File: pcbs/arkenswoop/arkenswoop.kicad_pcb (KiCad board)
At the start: 2 copper layers, 108.1 x 88.5 mm, 68 parts, among them J1 TRRS, SW1 Choc, SW10 Choc, SW11 Choc, SW12 Choc, SW13 Choc, SW14 Choc, SW15 Choc, SW16 Choc, SW17 Choc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

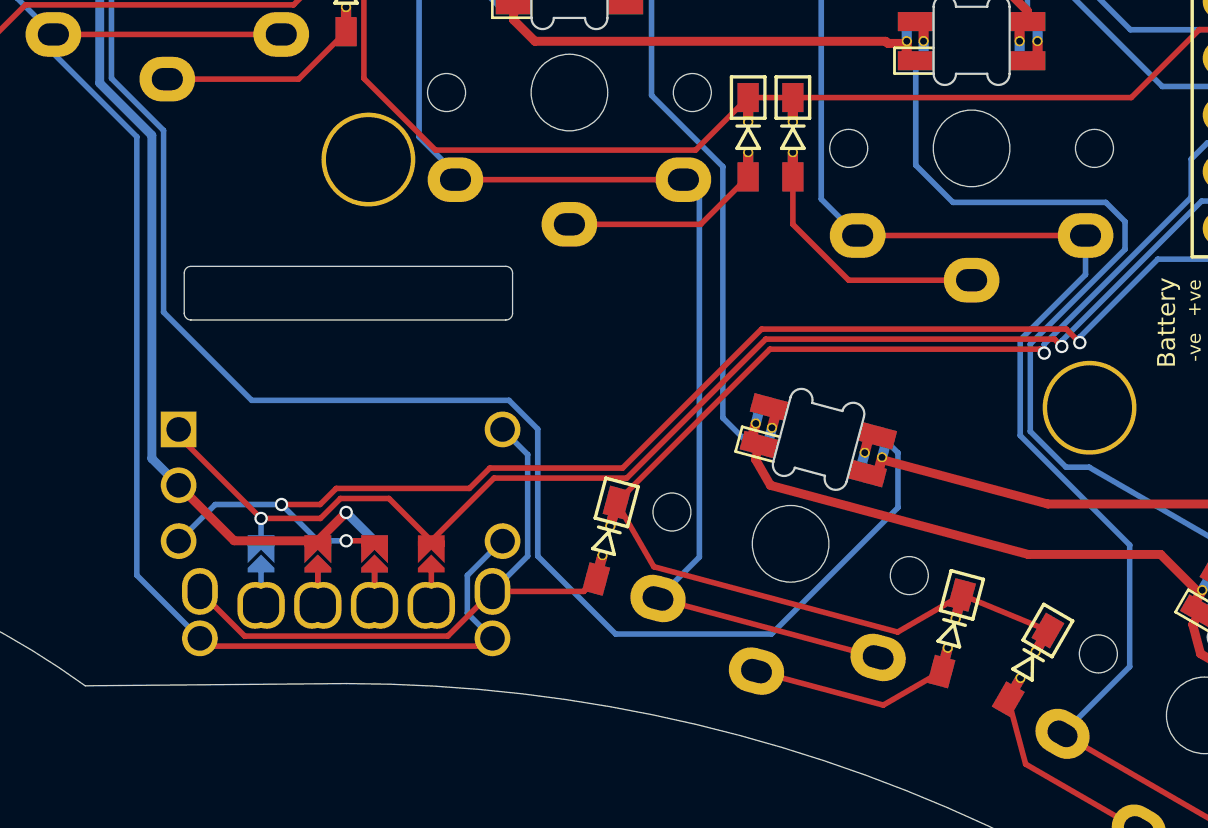
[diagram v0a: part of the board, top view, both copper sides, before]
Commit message: moving the encoder about 0.3mm down ; this should give enough clearance to the nearest key and its keycap
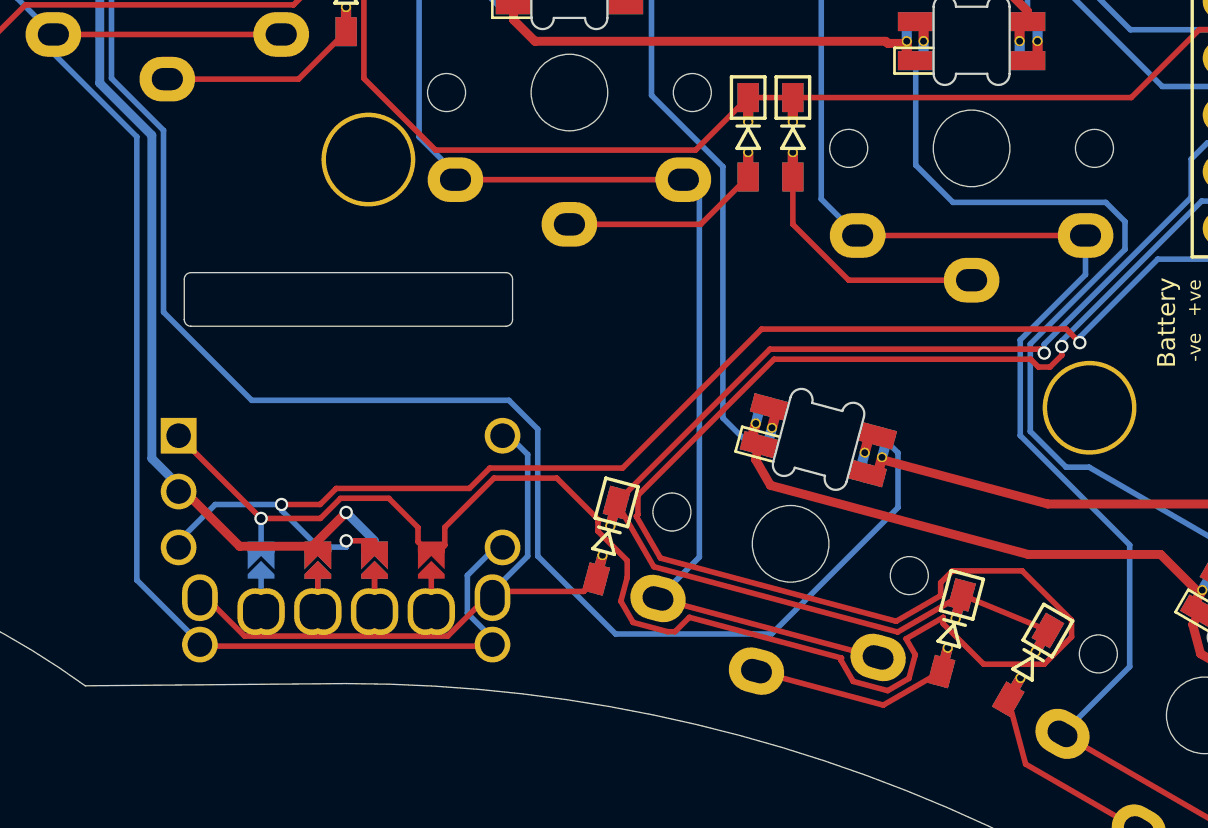
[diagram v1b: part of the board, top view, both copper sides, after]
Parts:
- moved EN1 0.28 mm to (115.2, 127.6)
- moved EN2 0.28 mm to (115.2, 127.6)
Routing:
- net eda: track 73.5 -> 129.1 mm
- net edb: track 74.2 -> 75.1 mm

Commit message: removed leds footprint
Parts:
- removed L1, L10, L11, L12, L13, L14, L15, L16, L17, L2, L3, L4, L5, L6, L7, L8, L9: SK6812Mini-e, swoop:SK6812_Mini_E
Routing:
- net VCC: track 394.7 -> 48.2 mm, vias 6 -> 3
- net GND: track 498.0 -> 160.6 mm, vias 8 -> 7
- net Net-(L13-Pad4): track 69.3 -> 0.00 mm
- net eda: track 129.1 -> 74.7 mm
- net led: track 63.9 -> 12.1 mm
- net Net-(L15-Pad4): track 42.9 -> 0.00 mm
- net Net-(L11-Pad4): track 35.2 -> 0.00 mm
- net Net-(L2-Pad4): track 31.0 -> 0.00 mm
- net Net-(L4-DIN): track 30.0 -> 0.00 mm
- net Net-(L14-Pad2): track 24.4 -> 0.00 mm
- net Net-(L14-Pad4): track 23.4 -> 0.00 mm
- net Net-(L2-Pad2): track 23.4 -> 0.00 mm
- net Net-(L4-Pad2): track 23.4 -> 0.00 mm
- net Net-(L12-Pad4): track 23.4 -> 0.00 mm
- net Net-(L10-Pad2): track 17.4 -> 0.00 mm
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
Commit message: customized pcb to have the jlcpcb order number under the mcu
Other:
- board text added: "Arkenswoop v0.5.0 https://github.com/SuperFola/arkenswoop"
- board text added: "JLCJLCJLCJLC"
- board text removed: "Arkenswoop v0.4.2 https://github.com/SuperFola/arkenswoop"
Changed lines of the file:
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@@
   (paper "A4")
   (title_block
-    (title "Swoop Choc")
-    (date "2023-05-28")
-    (rev "0.4.2")
-    (company "jmnw")
+    (title "Arkenswoop")
+    (date "2023-06-12")
+    (rev "0.5.0")
+    (company "SuperFola")
   )
   (layers
@@
   (gr_arc (start 80.677686 69.000074) (mid 81.223519 67.756064) (end 82.48217 67.244898)
     (stroke (width 0.05) (type solid)) (layer "Edge.Cuts"))
-  (gr_text "Arkenswoop v0.4.2\nhttps://github.com/SuperFola/arkenswoop" (at 163.188328 89.953937 90) (layer "B.SilkS")
+  (gr_text "Arkenswoop v0.5.0\nhttps://github.com/SuperFola/arkenswoop" (at 163.188328 89.953937 90) (layer "B.SilkS")
     (effects (font (size 0.8 0.8) (thickness 0.1)) (justify left mirror))
   )
-  (gr_text "Arkenswoop v0.4.2\nhttps://github.com/SuperFola/arkenswoop" (at 163.188327 114.013939 90) (layer "F.SilkS")
+  (gr_text "JLCJLCJLCJLC" (at 161.22 113.85 90) (layer "F.SilkS")
+    (effects (font (size 0.9 0.9) (thickness 0.1)) (justify left bottom))
+  )
+  (gr_text "Arkenswoop v0.5.0\nhttps://github.com/SuperFola/arkenswoop" (at 163.188327 114.013939 90) (layer "F.SilkS")
     (effects (font (size 0.8 0.8) (thickness 0.1)) (justify left))
   )

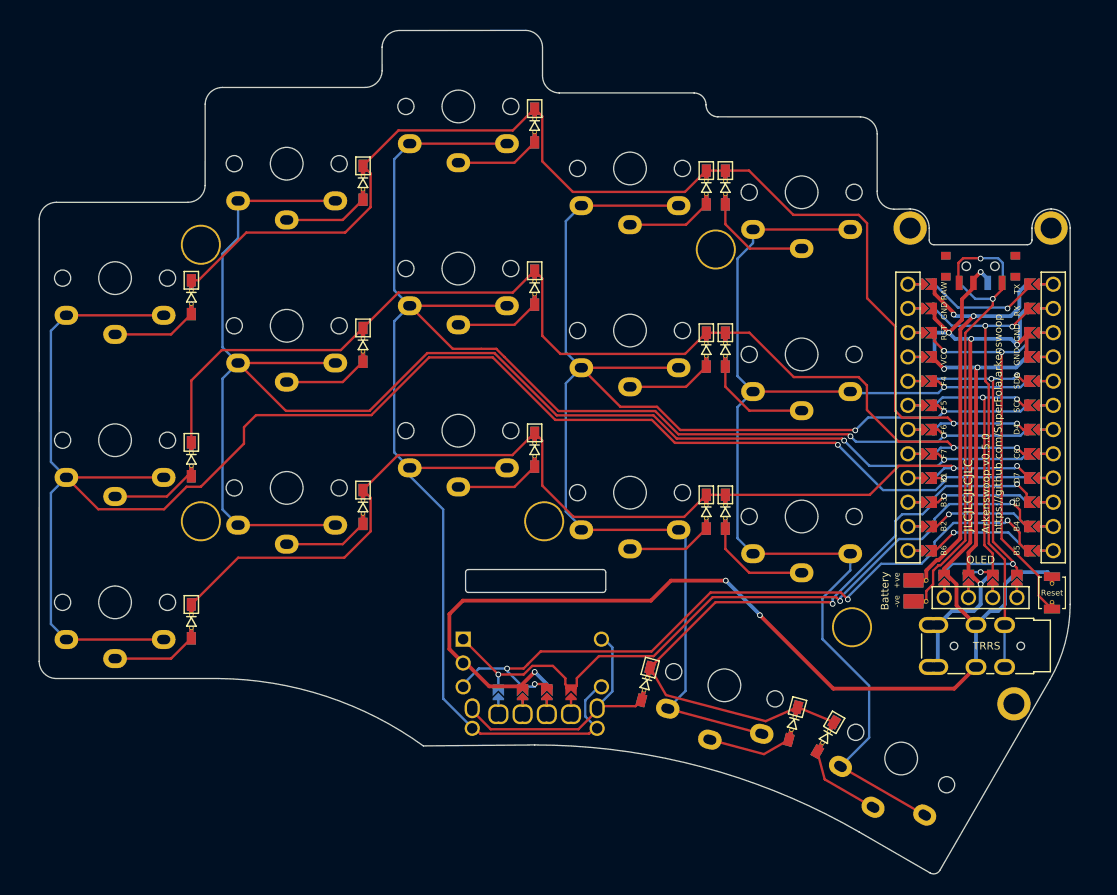
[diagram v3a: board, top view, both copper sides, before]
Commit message: removing old soldered version
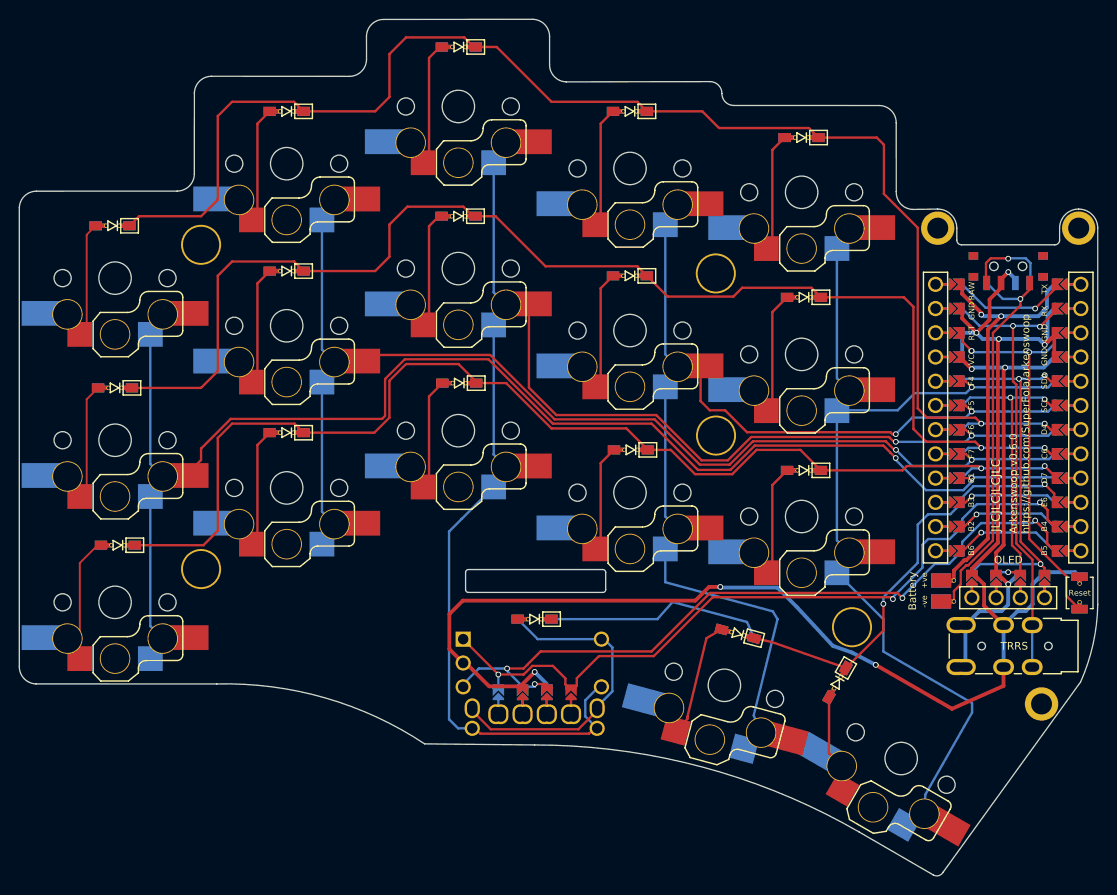
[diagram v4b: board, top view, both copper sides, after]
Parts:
- SW1, SW10, SW11, SW12, SW13, SW14, SW15, SW16, SW17, SW2, SW3, SW4, SW5, SW6, SW7, SW8, SW9: footprint swoop:Choc -> Library:Kailh-pg1350-socket-reversible
- moved H4 20.1 mm to (134.2, 103.8)
- moved ED1 13.5 mm to (115.2, 123.0), turned to 180 degrees
- moved D3 11.5 mm to (107.3, 63.0), turned to 180 degrees
- moved D4 11.3 mm to (125.2, 69.8), turned to 180 degrees
- moved D12 11.2 mm to (89.2, 103.5), turned to 180 degrees
- moved D1 11.1 mm to (71.0, 81.8), turned to 180 degrees
- moved D7 11.1 mm to (89.2, 86.5), turned to 180 degrees
- moved D9 11.1 mm to (125.2, 87.0), turned to 180 degrees
- moved D11 11.1 mm to (71.5, 115.2), turned to 180 degrees
- moved D16 11.0 mm to (136.5, 124.5), turned to 165 degrees
- moved D2 11.0 mm to (89.2, 69.8), turned to 180 degrees
- moved D6 11.0 mm to (71.2, 98.8), turned to 180 degrees
- moved D8 10.9 mm to (107.2, 80.8), turned to 180 degrees
- moved D13 10.6 mm to (107.3, 98.2), turned to 180 degrees
- moved D14 10.2 mm to (125.3, 105.2), turned to 180 degrees
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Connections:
- D1 pad 2: (no net) -> Net-(D1-A)
- D10 pad 2: (no net) -> Net-(D10-A)
- D11 pad 2: (no net) -> Net-(D11-A)
- D12 pad 2: (no net) -> Net-(D12-A)
- D13 pad 2: (no net) -> Net-(D13-A)
- D14 pad 2: (no net) -> Net-(D14-A)
- D15 pad 2: (no net) -> Net-(D15-A)
- D16 pad 2: (no net) -> Net-(D16-A)
- D17 pad 2: (no net) -> Net-(D17-A)
- D2 pad 2: (no net) -> Net-(D2-A)
- D3 pad 2: (no net) -> Net-(D3-A)
- D4 pad 2: (no net) -> Net-(D4-A)
- D5 pad 2: (no net) -> Net-(D5-A)
- D6 pad 2: (no net) -> Net-(D6-A)
- D7 pad 2: (no net) -> Net-(D7-A)
- D8 pad 2: (no net) -> Net-(D8-A)
- D9 pad 2: (no net) -> Net-(D9-A)
- SW1 pad : (no net) -> col0
- SW10 pad : (no net) -> col4
- SW11 pad : (no net) -> col0
- SW12 pad : (no net) -> col1
- SW13 pad : (no net) -> col2
- SW14 pad : (no net) -> col3
- SW15 pad : (no net) -> col4
- SW16 pad : (no net) -> col3
- SW17 pad : (no net) -> col4
- SW2 pad : (no net) -> col1
- SW3 pad : (no net) -> col2
- SW4 pad : (no net) -> col3
- SW5 pad : (no net) -> col4
- SW6 pad : (no net) -> col0
- SW7 pad : (no net) -> col1
- SW8 pad : (no net) -> col2
- SW9 pad : (no net) -> col3
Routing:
- net col1: track 161.3 -> 112.9 mm
- net col3: track 149.1 -> 104.1 mm
- net col0: track 184.6 -> 139.7 mm
- net col2: track 189.2 -> 149.8 mm
- net col4: track 124.9 -> 90.6 mm
- net row1: track 115.9 -> 134.2 mm
- net row0: track 129.3 -> 147.2 mm
- net row2: track 110.7 -> 123.3 mm
- net er0: track 28.5 -> 33.7 mm
- net Net-(D11-A): track 8.88 -> 13.2 mm
- net eda: track 74.7 -> 78.8 mm
- net Net-(D3-A): track 8.88 -> 12.9 mm
- net Net-(D4-A): track 8.88 -> 12.7 mm
- net GND: track 160.6 -> 164.2 mm
- net Net-(D12-A): track 8.88 -> 12.5 mm
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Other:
- board size 108.1 x 88.5 mm -> 113.1 x 89.8 mm
- board text added: "Arkenswoop v0.6.0 https://github.com/SuperFola/arkenswoop"
- board text removed: "Arkenswoop v0.5.0 https://github.com/SuperFola/arkenswoop"

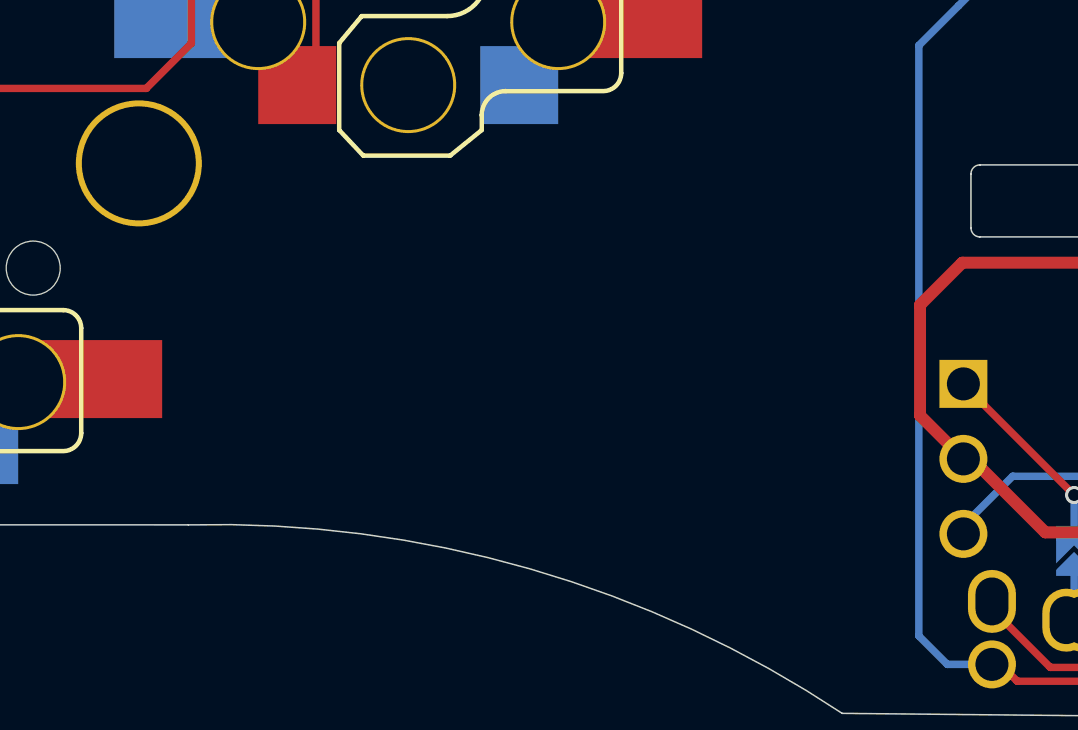
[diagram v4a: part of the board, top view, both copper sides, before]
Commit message: added silk on pcb
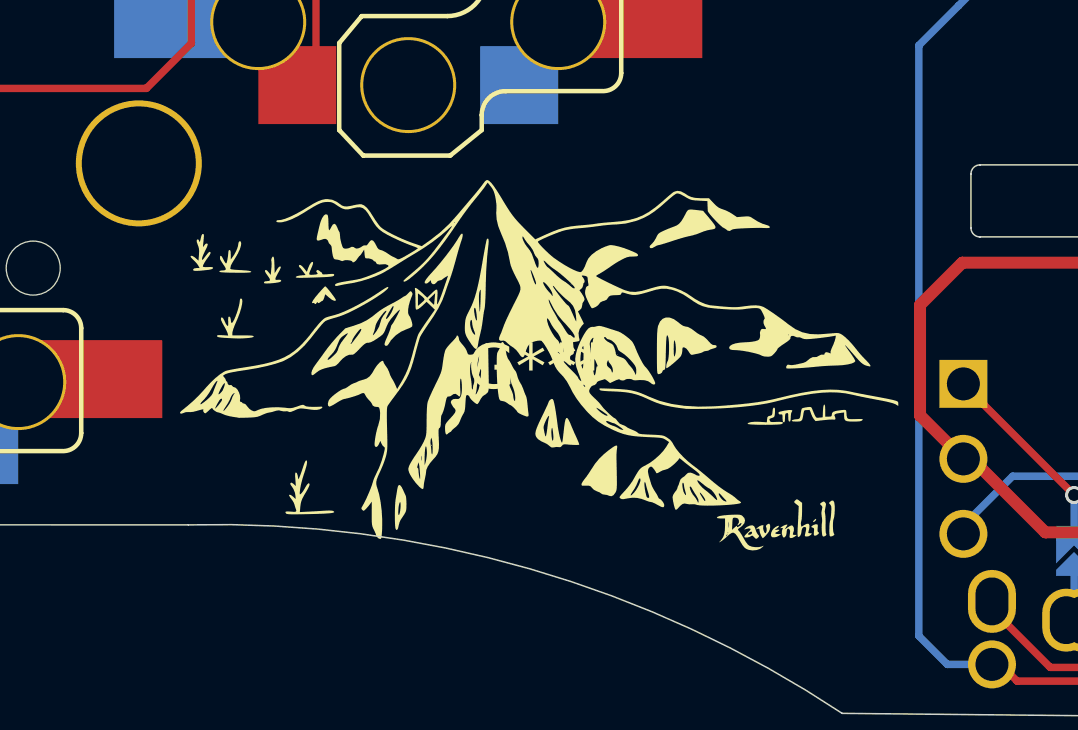
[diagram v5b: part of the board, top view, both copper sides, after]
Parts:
- added G***: LOGO, Library:erebor_silk, F.Cu at (93.5, 124.5)
